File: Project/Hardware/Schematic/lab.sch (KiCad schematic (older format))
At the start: 29 parts, among them J1 USB_B_Micro, J2 6P Male, J3 Conn_01x03_Male, U1 NCP1117-5.0_SOT223, U2 STM32F411RETx, U3 NCP1117-3.3_SOT223, Y1 8MHz

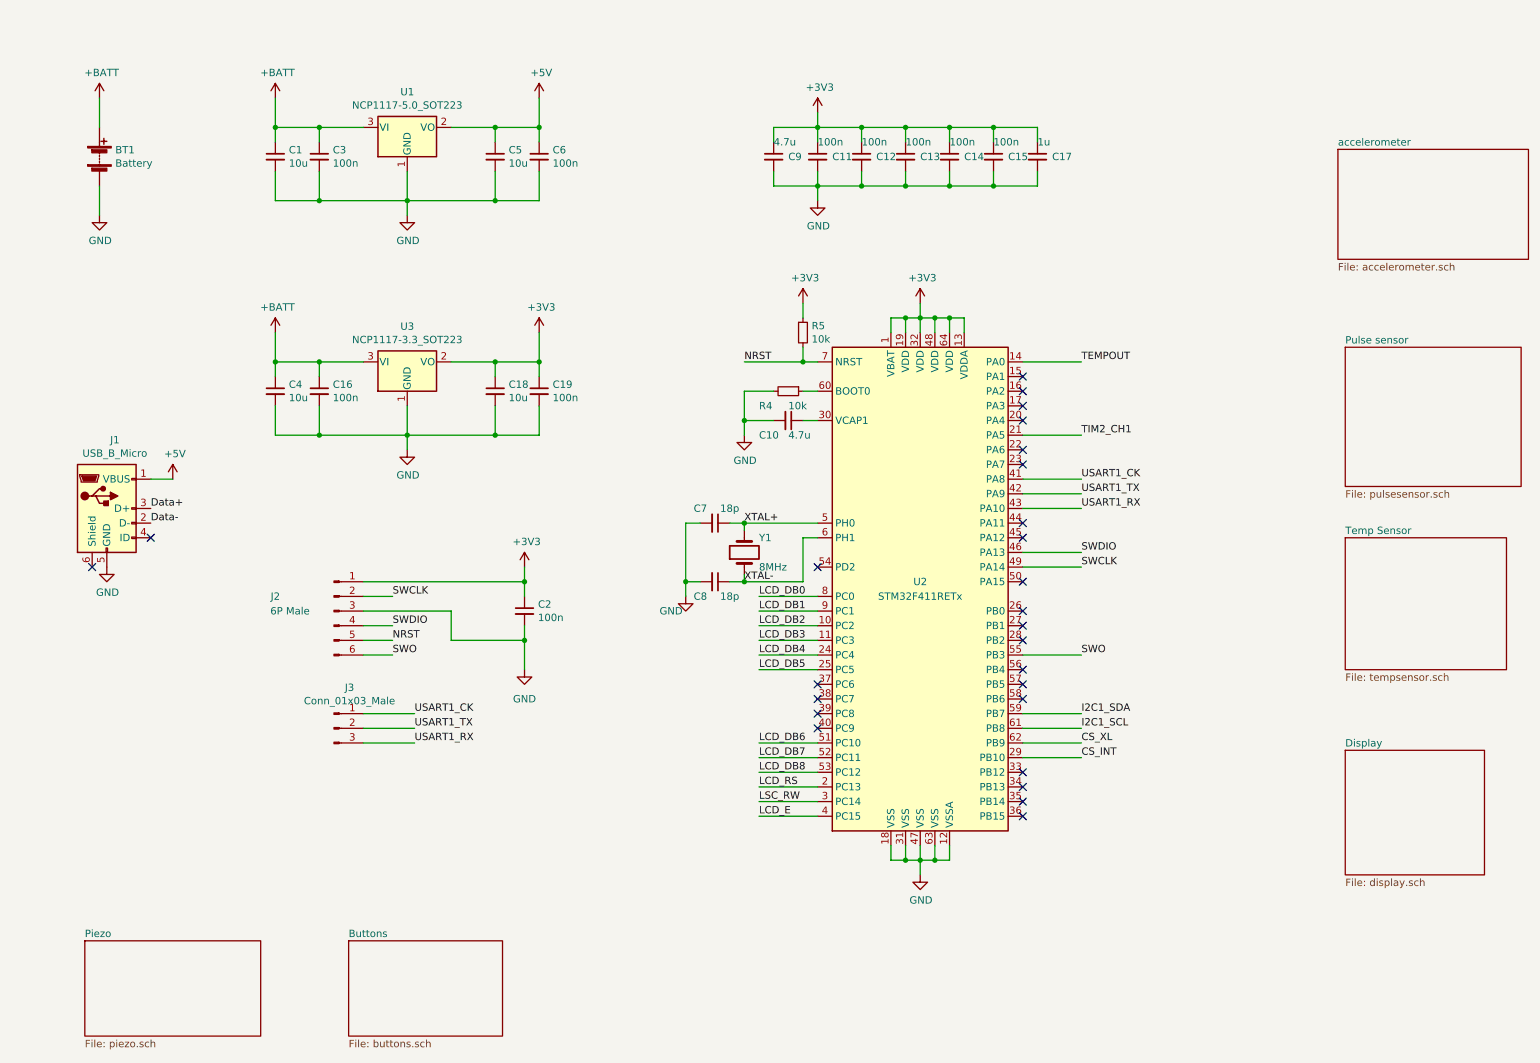
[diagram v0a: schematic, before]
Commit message: Pulse, piezo och labels (#8)
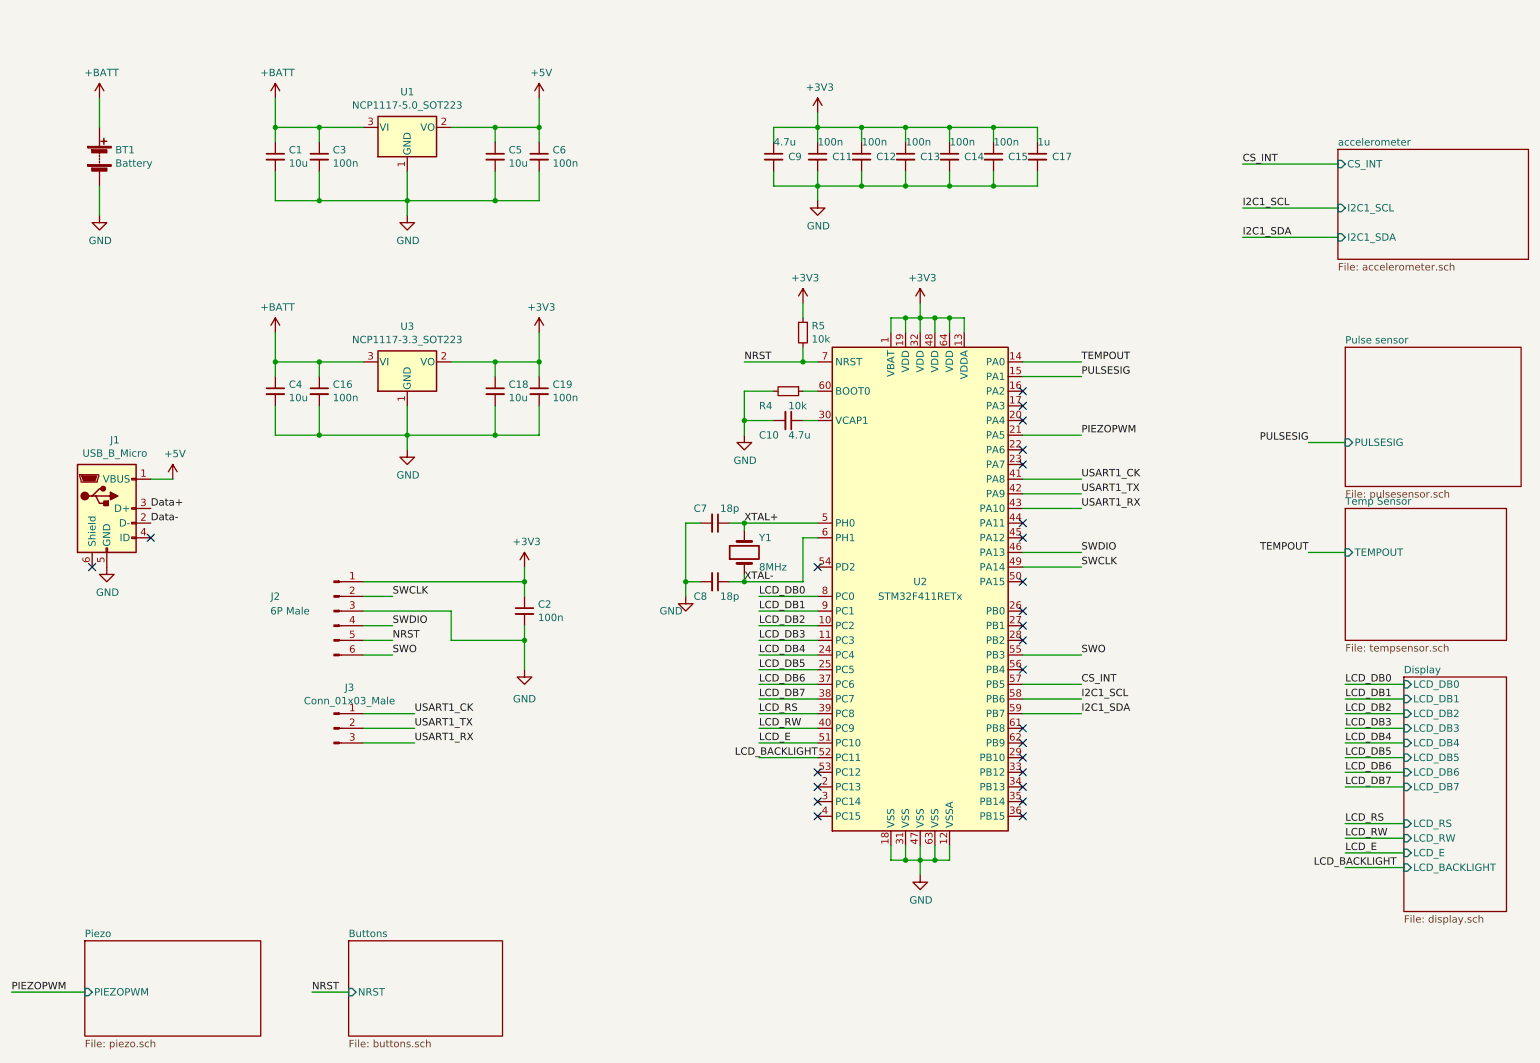
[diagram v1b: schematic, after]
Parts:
- J2: footprint Connector_PinHeader_2.54mm:PinHeader_1x06_P2.54mm_Vertical -> Pin_Headers:Pin_Header_Straight_1x06_Pitch2.54mm
- J3: footprint (none) -> Pin_Headers:Pin_Header_Straight_1x03_Pitch2.54mm
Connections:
- net CS_INT: now also U2.57 (PB5); no longer U2.29 (PB10)
- net I2C1_SCL: now also U2.58 (PB6); no longer U2.61 (PB8)
- net LCD_DB6: now also U2.37 (PC6); no longer U2.51 (PC10)
- net LCD_DB7: now also U2.38 (PC7); no longer U2.52 (PC11)
- net LCD_E: now also U2.51 (PC10); no longer U2.4 (PC15)
- net LCD_RS: now also U2.39 (PC8); no longer U2.2 (PC13)
- net PULSESIG: now reaches U2.15 (PA1)
- net LCD_RW: now reaches U2.40 (PC9)
- net CS_XL: no longer names the net of U2.62 (PB9)
- net LCD_DB8: no longer names the net of U2.53 (PC12)
- net LSC_RW: no longer names the net of U2.3 (PC14)
- net TIM2_CH1 renamed PIEZOPWM
- new net LCD_BACKLIGHT: U2.52 (PC11)
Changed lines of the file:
@@
 F 0 "J2" H 2400 4500 50  0000 C CNN
 F 1 "6P Male" H 2500 4400 50  0000 C CNN
-F 2 "Connector_PinHeader_2.54mm:PinHeader_1x06_P2.54mm_Vertical" H 2800 4400 50  0001 C CNN
+F 2 "Pin_Headers:Pin_Header_Straight_1x06_Pitch2.54mm" H 2800 4400 50  0001 C CNN
 F 3 "~" H 2800 4400 50  0001 C CNN
 	1    2800 4400
@@
 	4200 1100 4200 900
 Connection ~ 4200 1100
-NoConn ~ 7500 2800
 NoConn ~ 7500 2900
 NoConn ~ 7500 3000
@@
 NoConn ~ 7500 4500
 NoConn ~ 7500 4800
-NoConn ~ 7500 4900
-NoConn ~ 7500 5000
 NoConn ~ 7500 5500
 NoConn ~ 7500 5600
 NoConn ~ 7500 5700
 NoConn ~ 7500 5800
-NoConn ~ 6100 5200
-NoConn ~ 6100 5100
-NoConn ~ 6100 5000
-NoConn ~ 6100 4900
 NoConn ~ 6100 4100
 $Comp
@@
 F0 "accelerometer" 50
 F1 "accelerometer.sch" 50
+F2 "I2C1_SCL" I L 9650 1650 50
+F3 "I2C1_SDA" I L 9650 1850 50
+F4 "CS_INT" I L 9650 1350 50
 $EndSheet
 $Sheet
@@
 F0 "Pulse sensor" 50
 F1 "pulsesensor.sch" 50
+F2 "PULSESIG" I L 9700 3250 50
 $EndSheet
 $Sheet
-S 9700 3900 1100 900
+S 9700 3700 1100 900
 U 5C564F10
 F0 "Temp Sensor" 50
 F1 "tempsensor.sch" 50
+F2 "TEMPOUT" I L 9700 4000 50
 $EndSheet
 $Sheet
-S 9700 5350 950  850
+S 10100 4850 700  1600
 U 5C564F2E
 F0 "Display" 50
 F1 "display.sch" 50
+F2 "LCD_BACKLIGHT" I L 10100 6150 50
+F3 "LCD_RS" I L 10100 5850 50
+F4 "LCD_RW" I L 10100 5950 50
+F5 "LCD_E" I L 10100 6050 50
+F6 "LCD_DB0" I L 10100 4900 50
+F7 "LCD_DB1" I L 10100 5000 50
+F8 "LCD_DB2" I L 10100 5100 50
+F9 "LCD_DB3" I L 10100 5200 50
+F10 "LCD_DB4" I L 10100 5300 50
+F11 "LCD_DB5" I L 10100 5400 50
+F12 "LCD_DB6" I L 10100 5500 50
+F13 "LCD_DB7" I L 10100 5600 50
 $EndSheet
 $Sheet
@@
 F0 "Piezo" 50
 F1 "piezo.sch" 50
+F2 "PIEZOPWM" I L 1100 7000 50
 $EndSheet
 $Sheet
@@
 F0 "Buttons" 50
 F1 "buttons.sch" 50
+F2 "NRST" I L 2900 7000 50
 $EndSheet
 $Comp
@@
 I2C1_SDA
 Wire Wire Line
-	7500 5200 7900 5200
-Text Label 7900 5200 0    50   ~ 0
+	7500 5000 7900 5000
+Text Label 7900 5000 0    50   ~ 0
 I2C1_SCL
 Wire Wire Line
-	7500 5300 7900 5300
-Text Label 7900 5300 0    50   ~ 0
-CS_XL
-Wire Wire Line
-	7500 5400 7900 5400
-Text Label 7900 5400 0    50   ~ 0
-CS_INT
+	7500 4900 7900 4900
 Wire Wire Line
 	7500 2700 7900 2700
@@
 	7500 3200 7900 3200
 Text Label 7900 3200 0    50   ~ 0
-TIM2_CH1
+PIEZOPWM
 $Comp
 L Connector:Conn_01x03_Male J3
@@
 F 0 "J3" H 2906 5478 50  0000 C CNN
 F 1 "Conn_01x03_Male" H 2906 5387 50  0000 C CNN
-F 2 "" H 2800 5200 50  0001 C CNN
+F 2 "Pin_Headers:Pin_Header_Straight_1x03_Pitch2.54mm" H 2800 5200 50  0001 C CNN
 F 3 "~" H 2800 5200 50  0001 C CNN
 	1    2800 5200
@@
 Text Label 3350 5300 0    50   ~ 0
 USART1_RX
-Text Label 5700 4300 0    50   ~ 0
-LCD_DB0
 Text Label 5700 4400 0    50   ~ 0
 LCD_DB1
@@
 Text Label 5700 4800 0    50   ~ 0
 LCD_DB5
+Text Label 5700 4900 0    50   ~ 0
+LCD_DB6
+Text Label 5700 5000 0    50   ~ 0
+LCD_DB7
+Wire Wire Line
+	5700 4900 6100 4900
+Wire Wire Line
+	5700 5000 6100 5000
+Wire Wire Line
+	6100 5100 5700 5100
+Text Label 5700 5100 0    50   ~ 0
+LCD_RS
+Wire Wire Line
+	6100 5200 5700 5200
+Text Label 5700 5200 0    50   ~ 0
+LCD_RW
+Wire Wire Line
+	6100 5300 5700 5300
 Text Label 5700 5300 0    50   ~ 0
-LCD_DB6
-Text Label 5700 5400 0    50   ~ 0
-LCD_DB7
-Text Label 5700 5500 0    50   ~ 0
-LCD_DB8
-Wire Wire Line
-	5700 5300 6100 5300
-Wire Wire Line
-	5700 5400 6100 5400
-Wire Wire Line
-	5700 5500 6100 5500
-Wire Wire Line
-	6100 5600 5700 5600
-Text Label 5700 5600 0    50   ~ 0
-LCD_RS
-Wire Wire Line
-	6100 5700 5700 5700
-Text Label 5700 5700 0    50   ~ 0
-LSC_RW
-Wire Wire Line
-	6100 5800 5700 5800
-Text Label 5700 5800 0    50   ~ 0
 LCD_E
 $Comp
@@
 	1    0    0    -1
 $EndComp
+Wire Wire Line
+	7500 2800 7900 2800
+Text Label 7900 2800 0    50   ~ 0
+PULSESIG
+Text Label 7900 4900 0    50   ~ 0
+CS_INT
+NoConn ~ 7500 5400
+Text Label 6100 5400 2    50   ~ 0
+LCD_BACKLIGHT
+Wire Wire Line
+	6100 5400 5700 5400
+Wire Wire Line
+	9700 3250 9450 3250
+Text Label 9450 3250 2    50   ~ 0
+PULSESIG
+Wire Wire Line
+	9650 1650 9000 1650
+Text Label 9000 1650 0    50   ~ 0
+I2C1_SCL
+Wire Wire Line
+	9650 1850 9000 1850
+Text Label 9000 1850 0    50   ~ 0
+I2C1_SDA
+Wire Wire Line
+	9650 1350 9000 1350
+Text Label 9000 1350 0    50   ~ 0
+CS_INT
+NoConn ~ 7500 5300
+NoConn ~ 7500 5200
+Wire Wire Line
+	1100 7000 600  7000
+Text Label 600  7000 0    50   ~ 0
+PIEZOPWM
+Wire Wire Line
+	10100 4900 9700 4900
+Text Label 9700 4900 0    50   ~ 0
+LCD_DB0
+Wire Wire Line
+	10100 5000 9700 5000
+Text Label 9700 5000 0    50   ~ 0
+LCD_DB1
+Wire Wire Line
+	10100 5100 9700 5100
+Text Label 9700 5100 0    50   ~ 0
+LCD_DB2
+Wire Wire Line
+	10100 5200 9700 5200
+Text Label 9700 5200 0    50   ~ 0
+LCD_DB3
+Wire Wire Line
+	10100 5300 9700 5300
+Text Label 9700 5300 0    50   ~ 0
+LCD_DB4
+Wire Wire Line
+	10100 5400 9700 5400
+Text Label 9700 5400 0    50   ~ 0
+LCD_DB5
+Wire Wire Line
+	10100 5500 9700 5500
+Text Label 9700 5500 0    50   ~ 0
+LCD_DB6
+Wire Wire Line
+	10100 5600 9700 5600
+Text Label 9700 5600 0    50   ~ 0
+LCD_DB7
+Wire Wire Line
+	10100 5850 9700 5850
+Text Label 9700 5850 0    50   ~ 0
+LCD_RS
+Wire Wire Line
+	10100 5950 9700 5950
+Text Label 9700 5950 0    50   ~ 0
+LCD_RW
+Wire Wire Line
+	10100 6050 9700 6050
+Text Label 9700 6050 0    50   ~ 0
+LCD_E
+Wire Wire Line
+	10100 6150 9700 6150
+Text Label 10050 6150 2    50   ~ 0
+LCD_BACKLIGHT
+Wire Wire Line
+	9700 4000 9450 4000
+Text Label 9450 4000 2    50   ~ 0
+TEMPOUT
+NoConn ~ 6100 5600
+NoConn ~ 6100 5700
+NoConn ~ 6100 5800
+Wire Wire Line
+	2900 7000 2650 7000
+Text Label 2650 7000 0    50   ~ 0
+NRST
+Text Label 5700 4300 0    50   ~ 0
+LCD_DB0
+NoConn ~ 6100 5500
 $EndSCHEMATC

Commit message: Bytte display
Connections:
- net LCD_BACKLIGHT renamed LCD_RES
- net LCD_RS renamed LCD_DC
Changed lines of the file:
@@
 $EndSheet
 $Sheet
-S 9700 2600 1200 950
+S 9650 2200 1200 950
 U 5C564E6B
 F0 "Pulse sensor" 50
 F1 "pulsesensor.sch" 50
-F2 "PULSESIG" I L 9700 3250 50
+F2 "PULSESIG" I L 9650 2850 50
 $EndSheet
 $Sheet
-S 9700 3700 1100 900
+S 9650 3300 1100 900
 U 5C564F10
 F0 "Temp Sensor" 50
 F1 "tempsensor.sch" 50
-F2 "TEMPOUT" I L 9700 4000 50
+F2 "TEMPOUT" I L 9650 3600 50
 $EndSheet
 $Sheet
-S 10100 4850 700  1600
+S 9650 4400 700  1400
 U 5C564F2E
 F0 "Display" 50
 F1 "display.sch" 50
-F2 "LCD_BACKLIGHT" I L 10100 6150 50
-F3 "LCD_RS" I L 10100 5850 50
-F4 "LCD_RW" I L 10100 5950 50
-F5 "LCD_E" I L 10100 6050 50
-F6 "LCD_DB0" I L 10100 4900 50
-F7 "LCD_DB1" I L 10100 5000 50
-F8 "LCD_DB2" I L 10100 5100 50
-F9 "LCD_DB3" I L 10100 5200 50
-F10 "LCD_DB4" I L 10100 5300 50
-F11 "LCD_DB5" I L 10100 5400 50
-F12 "LCD_DB6" I L 10100 5500 50
-F13 "LCD_DB7" I L 10100 5600 50
+F2 "LCD_BACKLIGHT" I L 9650 5700 50
+F3 "LCD_RW" I L 9650 4750 50
+F4 "LCD_E" I L 9650 4650 50
+F5 "LCD_BS0" I L 9650 5300 50
+F6 "LCD_BS1" I L 9650 5400 50
+F7 "LCD_BS2" I L 9650 5500 50
+F8 "LCD_RES" I L 9650 5200 50
+F9 "LCD_DC" I L 9650 4550 50
+F10 "LCD_SDA" I L 9650 5050 50
+F11 "LCD_SCL" I L 9650 4900 50
 $EndSheet
 $Sheet
@@
 	6100 5100 5700 5100
 Text Label 5700 5100 0    50   ~ 0
-LCD_RS
+LCD_DC
 Wire Wire Line
 	6100 5200 5700 5200
@@
 CS_INT
 NoConn ~ 7500 5400
-Text Label 6100 5400 2    50   ~ 0
-LCD_BACKLIGHT
+Text Label 5700 5400 0    50   ~ 0
+LCD_RES
 Wire Wire Line
 	6100 5400 5700 5400
 Wire Wire Line
-	9700 3250 9450 3250
-Text Label 9450 3250 2    50   ~ 0
+	9650 2850 9400 2850
+Text Label 9400 2850 2    50   ~ 0
 PULSESIG
 Wire Wire Line
@@
 PIEZOPWM
 Wire Wire Line
-	10100 4900 9700 4900
-Text Label 9700 4900 0    50   ~ 0
-LCD_DB0
-Wire Wire Line
-	10100 5000 9700 5000
-Text Label 9700 5000 0    50   ~ 0
-LCD_DB1
-Wire Wire Line
-	10100 5100 9700 5100
-Text Label 9700 5100 0    50   ~ 0
-LCD_DB2
-Wire Wire Line
-	10100 5200 9700 5200
-Text Label 9700 5200 0    50   ~ 0
-LCD_DB3
-Wire Wire Line
-	10100 5300 9700 5300
-Text Label 9700 5300 0    50   ~ 0
-LCD_DB4
-Wire Wire Line
-	10100 5400 9700 5400
-Text Label 9700 5400 0    50   ~ 0
-LCD_DB5
-Wire Wire Line
-	10100 5500 9700 5500
-Text Label 9700 5500 0    50   ~ 0
-LCD_DB6
-Wire Wire Line
-	10100 5600 9700 5600
-Text Label 9700 5600 0    50   ~ 0
-LCD_DB7
-Wire Wire Line
-	10100 5850 9700 5850
-Text Label 9700 5850 0    50   ~ 0
-LCD_RS
-Wire Wire Line
-	10100 5950 9700 5950
-Text Label 9700 5950 0    50   ~ 0
-LCD_RW
-Wire Wire Line
-	10100 6050 9700 6050
-Text Label 9700 6050 0    50   ~ 0
-LCD_E
-Wire Wire Line
-	10100 6150 9700 6150
-Text Label 10050 6150 2    50   ~ 0
-LCD_BACKLIGHT
-Wire Wire Line
-	9700 4000 9450 4000
-Text Label 9450 4000 2    50   ~ 0
+	9650 3600 9400 3600
+Text Label 9400 3600 2    50   ~ 0
 TEMPOUT
 NoConn ~ 6100 5600
@@
 LCD_DB0
 NoConn ~ 6100 5500
+Wire Wire Line
+	9650 5050 9250 5050
+Text Label 9250 5050 0    50   ~ 0
+I2C1_SDA
+Wire Wire Line
+	9650 4900 9250 4900
+Text Label 9250 4900 0    50   ~ 0
+I2C1_SCL
+Text Label 9250 5200 0    50   ~ 0
+LCD_RES
+Wire Wire Line
+	9250 5200 9650 5200
 $EndSCHEMATC

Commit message: Ny display, igen!
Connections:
- net +5V: no longer C5.1, C6.1, U1.2 (VO)
- new net +12V: C5.1, C6.1, U1.2 (VO)
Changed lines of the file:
@@
 	3600 1100 3900 1100
 Connection ~ 3900 1100
-$Comp
-L power:+5V #PWR0112
-U 1 1 5C5E5791
-P 4200 900
-F 0 "#PWR0112" H 4200 750 50  0001 C CNN
-F 1 "+5V" H 4215 1073 50  0000 C CNN
-F 2 "" H 4200 900 50  0001 C CNN
-F 3 "" H 4200 900 50  0001 C CNN
-	1    4200 900
-	1    0    0    -1
-$EndComp
 Wire Wire Line
 	3900 1600 3300 1600
@@
 Wire Wire Line
 	9250 5200 9650 5200
+$Comp
+L power:+12V #PWR?
+U 1 1 5C679F70
+P 4200 900
+F 0 "#PWR?" H 4200 750 50  0001 C CNN
+F 1 "+12V" H 4215 1073 50  0000 C CNN
+F 2 "" H 4200 900 50  0001 C CNN
+F 3 "" H 4200 900 50  0001 C CNN
+	1    4200 900
+	1    0    0    -1
+$EndComp
 $EndSCHEMATC
